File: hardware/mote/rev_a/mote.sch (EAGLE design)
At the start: 135 parts, among them J1 TC2030-JLINK-L, J2 TC2030-JLINK-L, Q1 CSD22206W, Q10 CSD22206W, Q11 CSD22206W, Q2 CSD22206W, Q6 CSD22206W, Q7 CSD22206W, Q8 CSD22206W, Q9 CSD22206W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

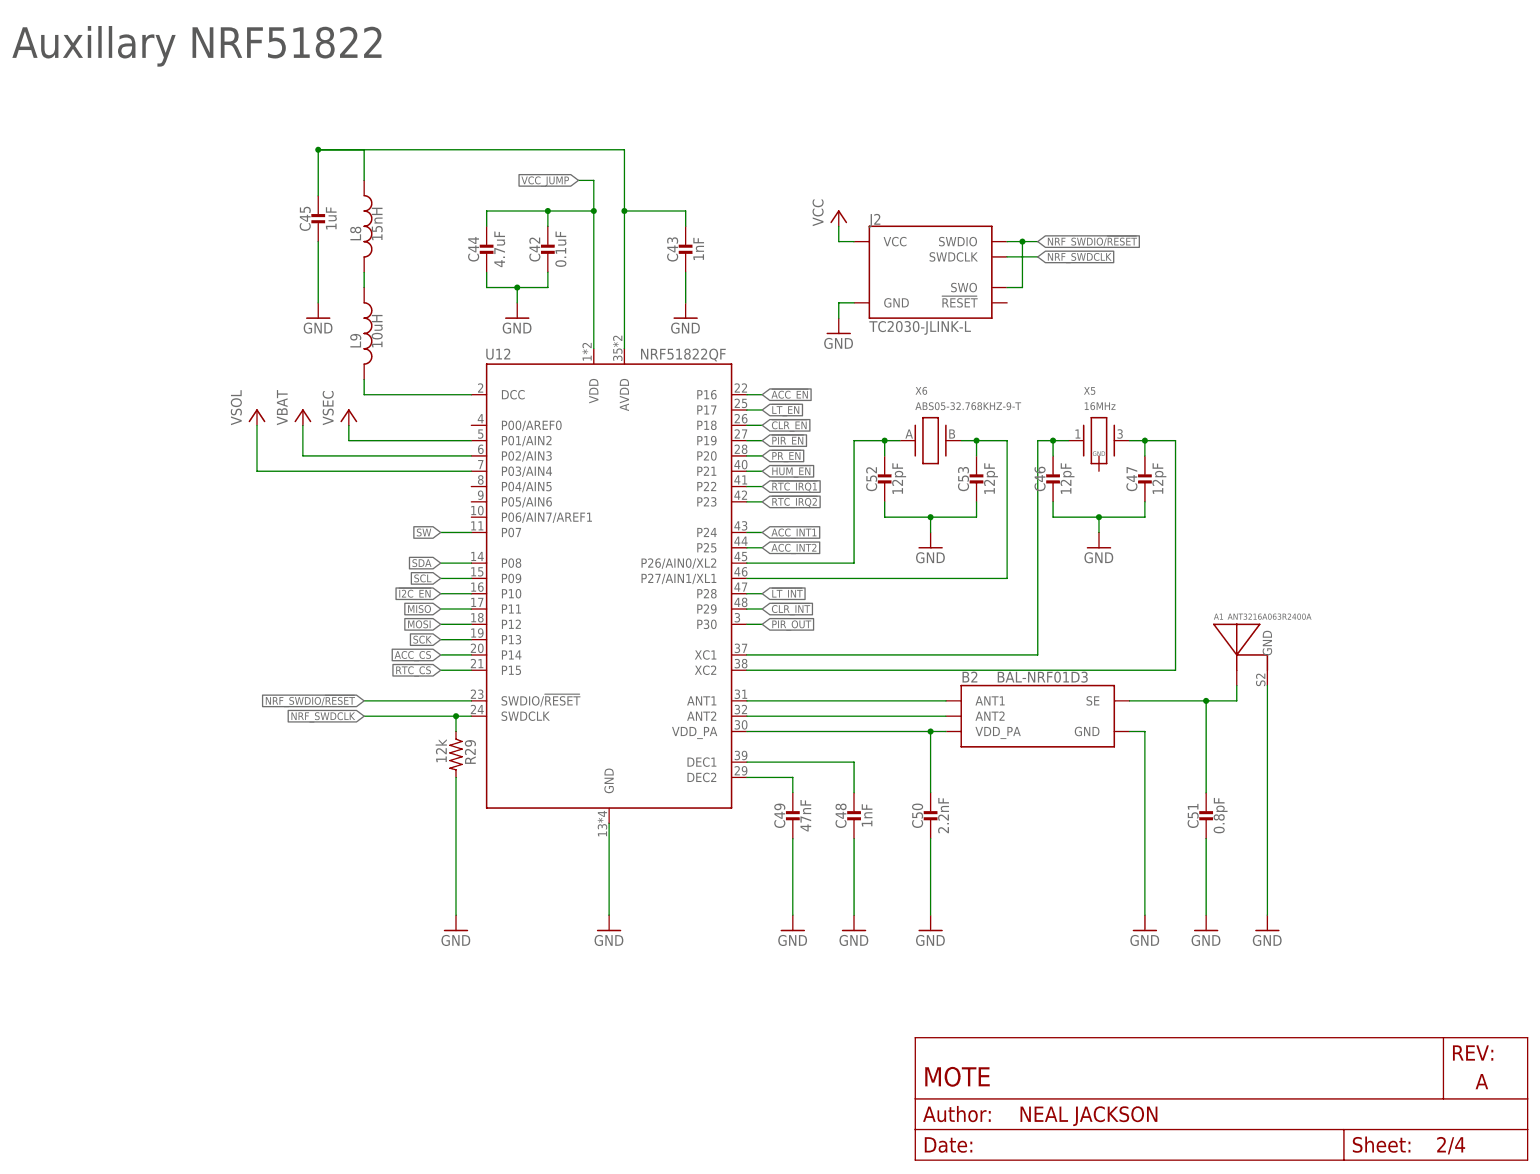
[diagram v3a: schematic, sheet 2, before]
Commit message: Majority of signals routed
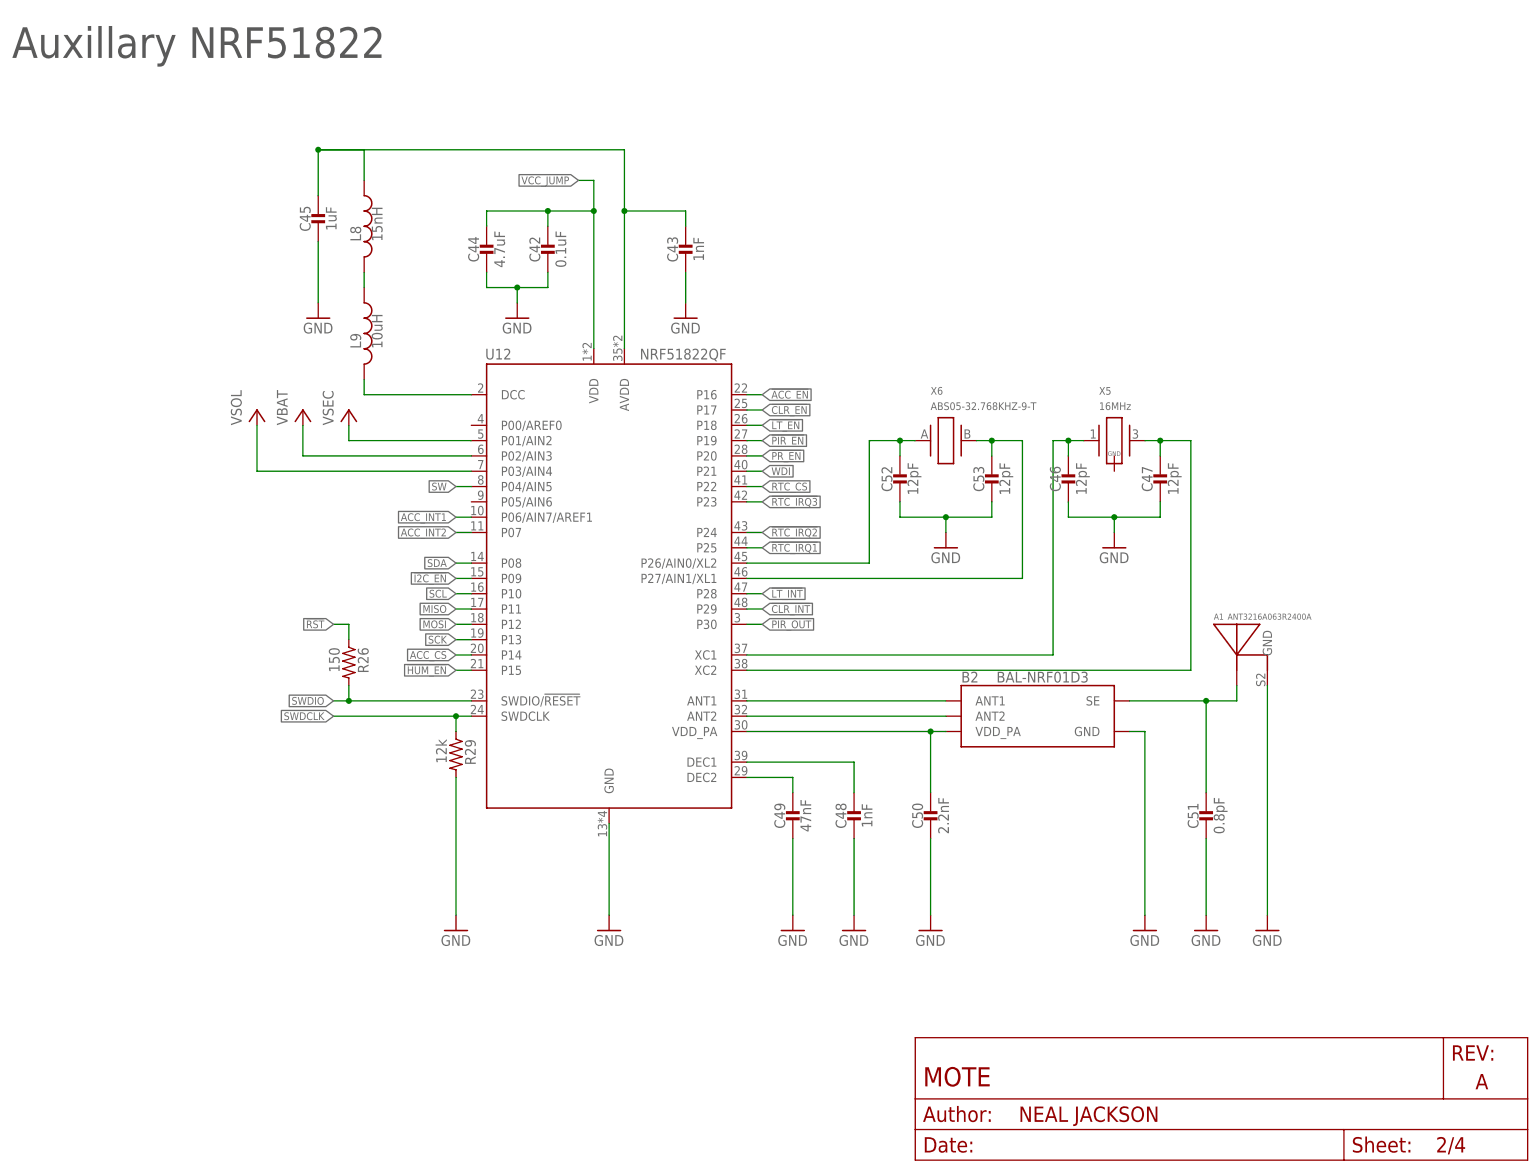
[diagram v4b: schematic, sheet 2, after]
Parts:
- removed J2: TC2030-JLINK-L, connector:TC2030-JLINK-L
- added R26: 150, passives:RESISTOR0402_RES
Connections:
- removed net N$28: J1.SWDIO, U1.SWDIO
- removed net N$29: J1.SWDCLK, U1.SWDCLK
- removed net NRF_SWDCLK: J2.SWDCLK, R29.1, U12.SWDCLK
- removed net NRF_SWDIO/!RESET: J2.SWDIO, J2.SWO, U12.SWDIO/!RESET
- new net SWDCLK: J1.SWDCLK, R29.1, U1.SWDCLK, U12.SWDCLK
- new net SWDIO: J1.SWDIO, J1.SWO, R26.2, U1.SWDIO, U12.SWDIO/!RESET
- net !CLR_EN: now also U12.P17; no longer U12.P18
- net !HUM_EN: now also U12.P15; no longer U12.P21
- net !I2C_EN: now also U12.P09; no longer U12.P10
- net !LT_EN: now also U12.P18; no longer U12.P17
- net !RST: now also R26.1
- net !RTC_IRQ1: now also U12.P25; no longer U12.P22
- net !RTC_IRQ2: now also U12.P24; no longer U12.P23
- net !RTC_IRQ3: now also U12.P23
- net ACC_INT1: now also U12.P06/AIN7/AREF1; no longer U12.P24
- net ACC_INT2: now also U12.P07; no longer U12.P25
- net GND: no longer J2.GND
- net RTC_CS: now also U12.P22; no longer U12.P15
- net SCL: now also U12.P10; no longer U12.P09
- net SW: now also U12.P04/AIN5; no longer U12.P07
- net VCC: no longer J2.VCC
- net WDI: now also U1.P0.31/AIN7, U12.P21
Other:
- note added: "Only populate one MCU! Either populate the NRF52840 (Page 1) or NRF51822 (Page 2)"
- moved on the sheet: C46, C47, C52, C53, X5, X6

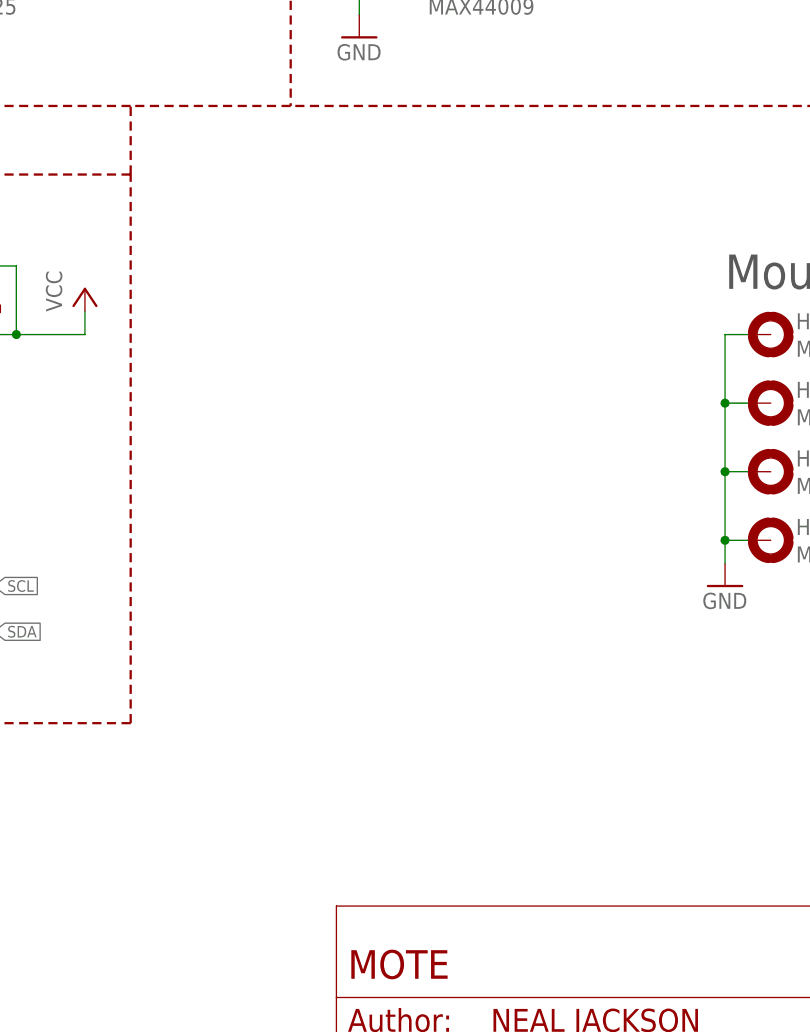
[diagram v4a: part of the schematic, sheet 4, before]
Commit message: Nothing to do! All signals routed
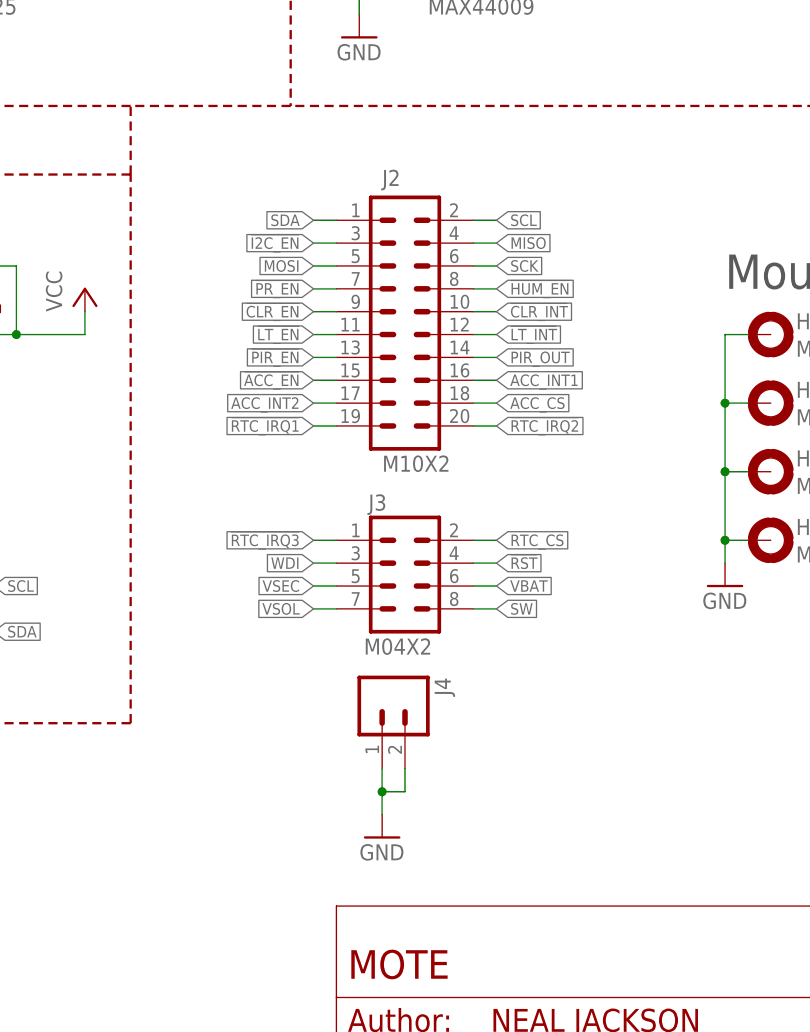
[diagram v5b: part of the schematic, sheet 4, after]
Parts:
- removed TP1, TP11, TP26, TP27: TEST_POINT_0.040IN, headers:TEST_POINT_0.040IN
- added J2: M10X2, SparkFun-Connectors:M10X2
- added J3: M04X2, SparkFun-Connectors:M04X2
- added J4: (no value), SparkFun-Connectors:M02PTH
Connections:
- net !ACC_EN: now also J2.15
- net !CLR_EN: now also J2.9
- net !CLR_INT: now also J2.10
- net !HUM_EN: now also J2.8
- net !I2C_EN: now also J2.3
- net !LT_EN: now also J2.11
- net !LT_INT: now also J2.12
- net !PIR_EN: now also J2.13
- net !PR_EN: now also J2.7
- net !RST: now also J3.4
- net !RTC_IRQ1: now also J2.19
- net !RTC_IRQ2: now also J2.20
- net !RTC_IRQ3: now also J3.1
- net ACC_CS: now also J2.18
- net ACC_INT1: now also J2.16
- net ACC_INT2: now also J2.17
- net GND: now also J4.1, J4.2; no longer TP26.TESTPOINT, TP27.TESTPOINT
- net MISO: now also J2.4
- net MOSI: now also J2.5
- net PIR_OUT: now also J2.14
- net RTC_CS: now also J3.2
- net SCK: now also J2.6
- net SCL: now also J2.2
- net SDA: now also J2.1
- net SW: now also J3.8; no longer TP11.TESTPOINT
- net VBAT: now also J3.6
- net VSEC: now also J3.5
- net VSOL: now also J3.7; no longer TP1.TESTPOINT
- net WDI: now also J3.3

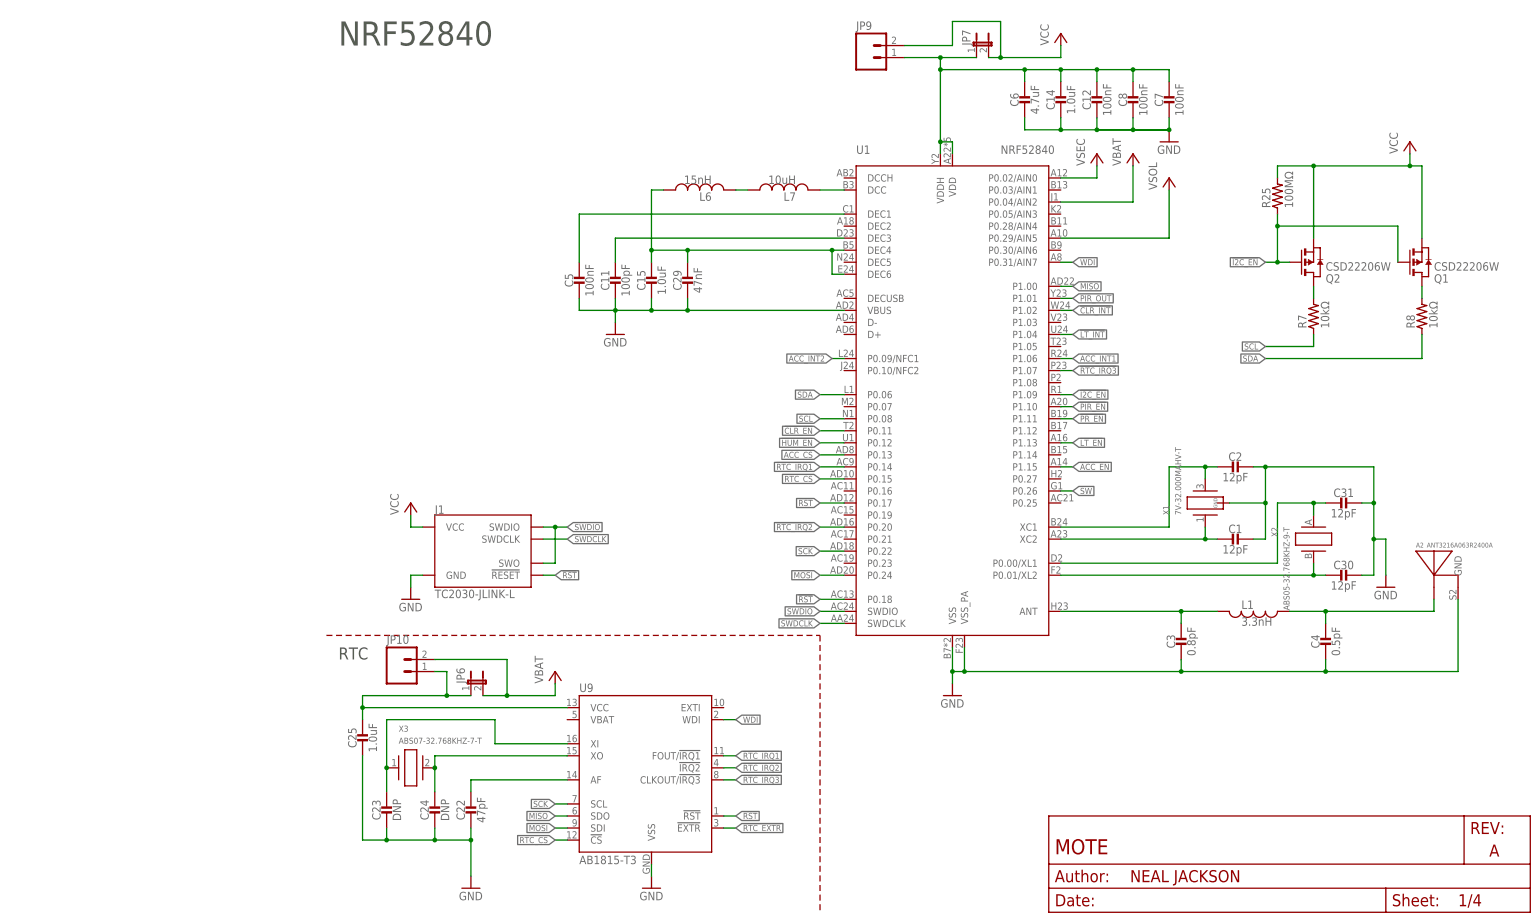
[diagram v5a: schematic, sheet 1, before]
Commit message: Add external reset button
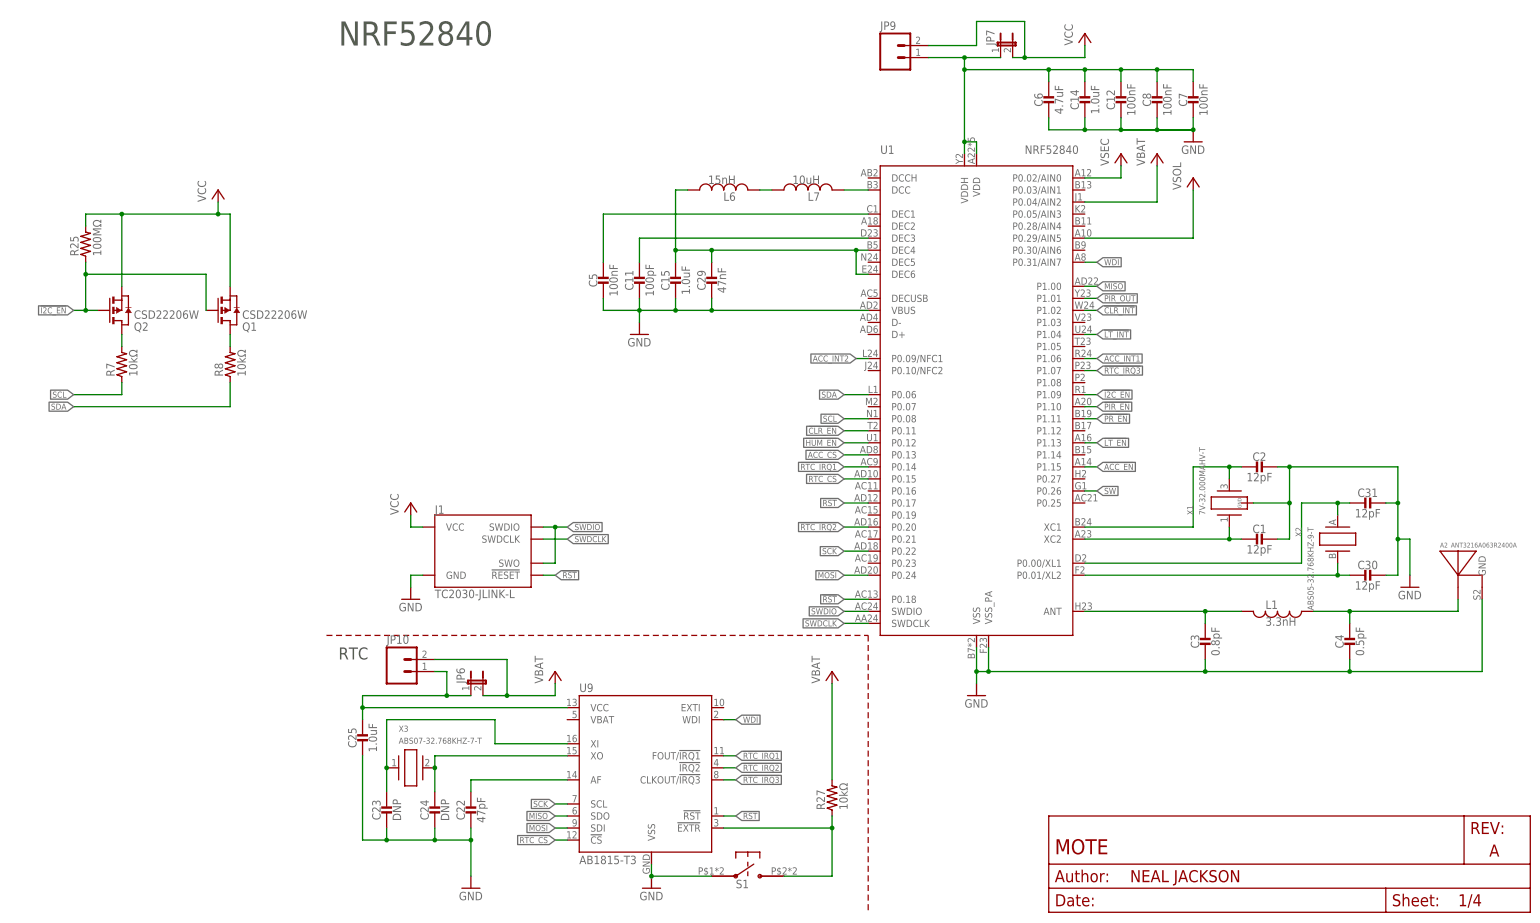
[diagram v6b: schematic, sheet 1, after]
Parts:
- added R27: 10kΩ, passives:RESISTOR0402_RES
- added S1: EVQP2, switches:EVQP2
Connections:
- net !RTC_EXTR: now also R27.1, S1.P$2
- net GND: now also S1.P$1
- net VBAT: now also R27.2
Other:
- moved on the sheet: A2, C1, C11, C12, C14, C15, C2, C29, C3, C30, C31, C4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

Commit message: Branden's fixes
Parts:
- added R28: 10kΩ, passives:RESISTOR0402_RES
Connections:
- net !RST: now also R28.1
- net VBAT: now also R28.2
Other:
- moved on the sheet: A2, C1, C11, C12, C14, C15, C2, C29, C3, C30, C31, C4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

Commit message: Add pfet for i2c isolation per sensor
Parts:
- removed Q6: CSD22206W, fets:CSD22206W
- removed R25, R9: 100MΩ, passives:RESISTOR0402_RES
- removed U4: AMN41121, chips:AMN41121
- added Q3, Q4: PMDXB950UPEL, fets:PMDXB950UPEL
- added U2: EKMB1101111, chips:EKMB1101111
- Q1, Q2: value CSD22206W -> PMDXB950UPEL; device fets:CSD22206W -> fets:PMDXB950UPEL
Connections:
- removed net N$40: C17.1, C9.1, JP1.1, JP11.1, Q6.S, R9.2
- new net N$48: Q2.2.D, U5.SDA
- new net N$50: Q2.1.D, U5.SCL
- new net N$51: Q3.2.D, U7.SDA
- new net N$52: Q3.1.D, U7.SCL
- new net N$54: Q4.2.D, U6.SDA
- new net N$55: Q4.1.D, U6.SCL
- net !ACC_EN: no longer Q6.G, R9.1
- net !CLR_EN: now also Q4.1.G, Q4.2.G
- net !HUM_EN: now also Q2.1.G, Q2.2.G
- net !I2C_EN: no longer Q1.G, Q2.G, R25.1, U1.P1.09, U12.P09
- net !LT_EN: now also Q3.1.G, Q3.2.G
- net !PR_EN: now also Q1.1.G, Q1.2.G
- net GND: now also U2.GND; no longer U4.GND
- net N$15: now also C17.1, C9.1, JP1.1, JP11.1; no longer Q6.D
- net N$23: now also U2.VCC; no longer U4.VCC
- net N$34: now also Q1.1.D, U10.SCL; no longer Q2.D, R7.2
- net N$41: now also Q1.2.D, U10.SDA; no longer Q1.D, R8.2
- net PIR_OUT: now also U2.OUT; no longer U4.OUT
- net SCL: now also Q1.1.S, Q2.1.S, Q3.1.S, Q4.1.S; no longer U10.SCL, U5.SCL, U6.SCL, U7.SCL
- net SDA: now also Q1.2.S, Q2.2.S, Q3.2.S, Q4.2.S; no longer U10.SDA, U5.SDA, U6.SDA, U7.SDA
- net VCC: now also R7.2, R8.2; no longer Q1.S, Q2.S, R25.2
